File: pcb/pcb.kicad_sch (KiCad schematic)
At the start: 90 parts, among them J1 OLED, SW1 RotaryEncoder_Switch, U1 Elite-C

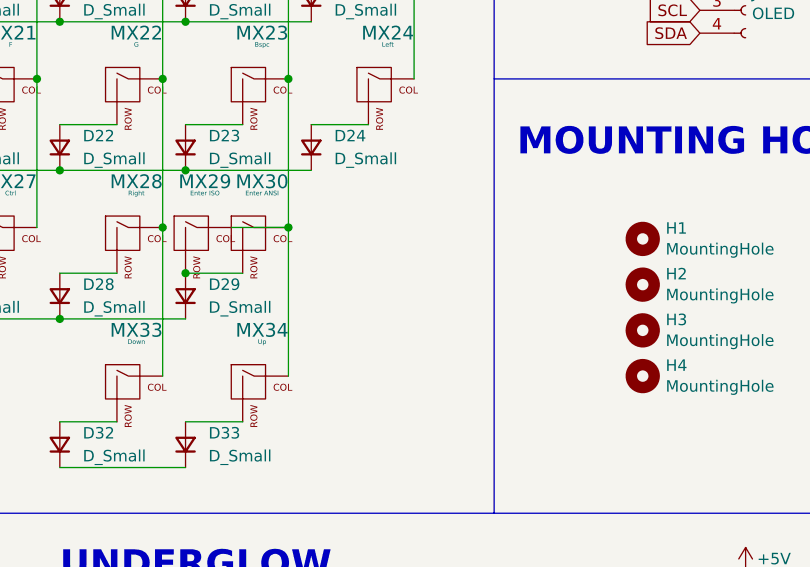
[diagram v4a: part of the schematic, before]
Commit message: Added footprints for most of the parts to the PCB file.
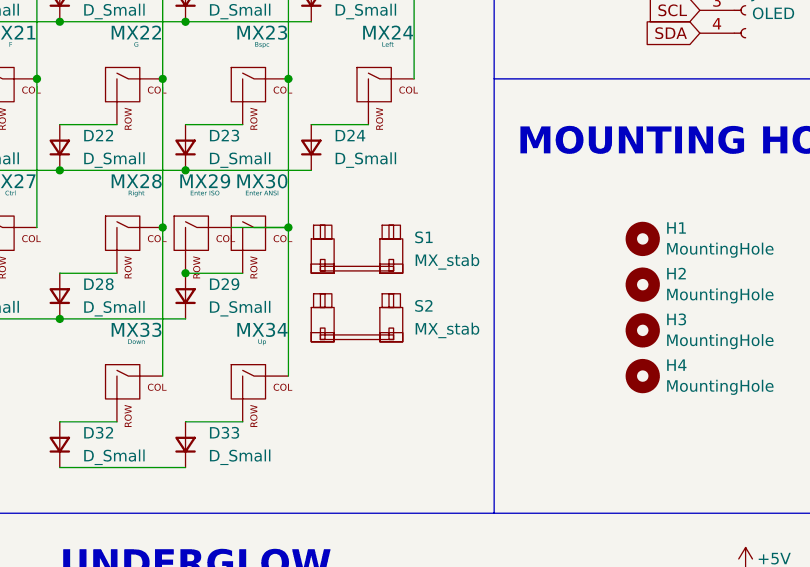
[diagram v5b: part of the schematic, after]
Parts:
- added S1: MX_stab, marbastlib-mx:STAB_MX_2.25u, symbol marbastlib-mx:MX_stab
- added S2: MX_stab, marbastlib-mx:STAB_MX_ISO_FLIPPED, symbol marbastlib-mx:MX_stab
- MX13, MX25, MX32: footprint acheron_MXH_metalrings:MX100H -> acheron_MXH_metalrings:MX125H
- MX26: footprint acheron_MXH_metalrings:MX100H -> acheron_MXH_metalrings:MX200H
- SW1: footprint Rotary_Encoder:RotaryEncoder_Alps_EC11E-Switch_Vertical_H20mm -> Keebio-Parts:RotaryEncoder_EC11-no-legs
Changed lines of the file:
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@@
       (effects (font (size 0.508 0.508)))
     )
-    (property "Footprint" "acheron_MXH_metalrings:MX100H" (id 2) (at 38.735 104.775 0)
+    (property "Footprint" "acheron_MXH_metalrings:MX200H" (id 2) (at 38.735 104.775 0)
       (effects (font (size 1.524 1.524)) hide)
     )
@@
     (pin "2")
   )
+  (symbol (lib_id "marbastlib-mx:MX_stab") (at 107.95 113.03 0) (unit 1)
+    (in_bom yes) (on_board yes) (fields_autoplaced)
+    (property "Reference" "S2" (id 0) (at 114.3 111.6329 0)
+      (effects (font (size 1.27 1.27)) (justify left))
+    )
+    (property "Value" "MX_stab" (id 1) (at 114.3 114.1729 0)
+      (effects (font (size 1.27 1.27)) (justify left))
+    )
+    (property "Footprint" "marbastlib-mx:STAB_MX_ISO_FLIPPED" (id 2) (at 107.95 113.03 0)
+      (effects (font (size 1.27 1.27)) hide)
+    )
+    (property "Datasheet" "" (id 3) (at 107.95 113.03 0)
+      (effects (font (size 1.27 1.27)) hide)
+    )
+  )
   (symbol (lib_id "MX_Alps_Hybrid:MX-NoLED") (at 96.52 54.61 0) (unit 1)
     (in_bom yes) (on_board yes) (fields_autoplaced)
@@
       (effects (font (size 0.508 0.508)))
     )
-    (property "Footprint" "acheron_MXH_metalrings:MX100H" (id 2) (at 24.765 71.755 0)
+    (property "Footprint" "acheron_MXH_metalrings:MX125H" (id 2) (at 24.765 71.755 0)
       (effects (font (size 1.524 1.524)) hide)
     )
@@
       (effects (font (size 0.508 0.508)))
     )
-    (property "Footprint" "acheron_MXH_metalrings:MX100H" (id 2) (at 24.765 104.775 0)
+    (property "Footprint" "acheron_MXH_metalrings:MX125H" (id 2) (at 24.765 104.775 0)
       (effects (font (size 1.524 1.524)) hide)
     )
@@
     (pin "1")
   )
+  (symbol (lib_id "marbastlib-mx:MX_stab") (at 107.95 105.41 0) (unit 1)
+    (in_bom yes) (on_board yes) (fields_autoplaced)
+    (property "Reference" "S1" (id 0) (at 114.3 104.0129 0)
+      (effects (font (size 1.27 1.27)) (justify left))
+    )
+    (property "Value" "MX_stab" (id 1) (at 114.3 106.5529 0)
+      (effects (font (size 1.27 1.27)) (justify left))
+    )
+    (property "Footprint" "marbastlib-mx:STAB_MX_2.25u" (id 2) (at 107.95 105.41 0)
+      (effects (font (size 1.27 1.27)) hide)
+    )
+    (property "Datasheet" "" (id 3) (at 107.95 105.41 0)
+      (effects (font (size 1.27 1.27)) hide)
+    )
+  )
   (symbol (lib_id "power:+5V") (at 151.13 140.97 0) (unit 1)
     (in_bom yes) (on_board yes)
@@
     (property "Reference" "SW1" (id 0) (at 144.78 30.48 0))
     (property "Value" "RotaryEncoder_Switch" (id 1) (at 144.78 33.02 0))
-    (property "Footprint" "Rotary_Encoder:RotaryEncoder_Alps_EC11E-Switch_Vertical_H20mm" (id 2) (at 148.59 44.704 0)
+    (property "Footprint" "Keebio-Parts:RotaryEncoder_EC11-no-legs" (id 2) (at 148.59 44.704 0)
       (effects (font (size 1.27 1.27)) hide)
     )
@@
       (effects (font (size 0.508 0.508)))
     )
-    (property "Footprint" "acheron_MXH_metalrings:MX100H" (id 2) (at 38.735 121.285 0)
+    (property "Footprint" "acheron_MXH_metalrings:MX125H" (id 2) (at 38.735 121.285 0)
       (effects (font (size 1.524 1.524)) hide)
     )
@@
     )
     (path "/3152788b-a0de-4109-8434-55ba1d4fe4a7"
-      (reference "MX13") (unit 1) (value "Shift") (footprint "acheron_MXH_metalrings:MX100H")
+      (reference "MX13") (unit 1) (value "Shift") (footprint "acheron_MXH_metalrings:MX125H")
     )
     (path "/46877c3a-ead4-41c8-afcb-24c8e59e5bae"
@@
     )
     (path "/553d3b6b-36a3-45b9-a24e-6f1c7c1abfbb"
-      (reference "MX25") (unit 1) (value "Alt") (footprint "acheron_MXH_metalrings:MX100H")
+      (reference "MX25") (unit 1) (value "Alt") (footprint "acheron_MXH_metalrings:MX125H")
     )
     (path "/152b7b17-3a42-4de5-b9bc-bdd22f42c43b"
-      (reference "MX26") (unit 1) (value "Space") (footprint "acheron_MXH_metalrings:MX100H")
+      (reference "MX26") (unit 1) (value "Space") (footprint "acheron_MXH_metalrings:MX200H")
     )
     (path "/d49df2b5-b3d2-431c-82f1-b1e8d86ff7d8"
@@
     )
     (path "/e3b59c53-ccff-4bc2-b7b7-efe6efe4c5cc"
-      (reference "MX32") (unit 1) (value "Alt") (footprint "acheron_MXH_metalrings:MX100H")
+      (reference "MX32") (unit 1) (value "Alt") (footprint "acheron_MXH_metalrings:MX125H")
     )
     (path "/5b6c7f1e-f125-477d-8e10-4610f8169c66"
@@
       (reference "MX34") (unit 1) (value "Up") (footprint "acheron_MXH_metalrings:MX100H")
     )
+    (path "/7ed119b7-b4ae-4245-9c6d-905d8f015e10"
+      (reference "S1") (unit 1) (value "MX_stab") (footprint "marbastlib-mx:STAB_MX_2.25u")
+    )
+    (path "/2fce2717-c9bf-487d-a03f-ec3953ab514e"
+      (reference "S2") (unit 1) (value "MX_stab") (footprint "marbastlib-mx:STAB_MX_ISO_FLIPPED")
+    )
     (path "/b0099de3-5821-425e-97d9-b89f55184911"
-      (reference "SW1") (unit 1) (value "RotaryEncoder_Switch") (footprint "Rotary_Encoder:RotaryEncoder_Alps_EC11E-Switch_Vertical_H20mm")
+      (reference "SW1") (unit 1) (value "RotaryEncoder_Switch") (footprint "Keebio-Parts:RotaryEncoder_EC11-no-legs")
     )
     (path "/45e43045-7dd0-4e88-82a6-613fa4322bc2"

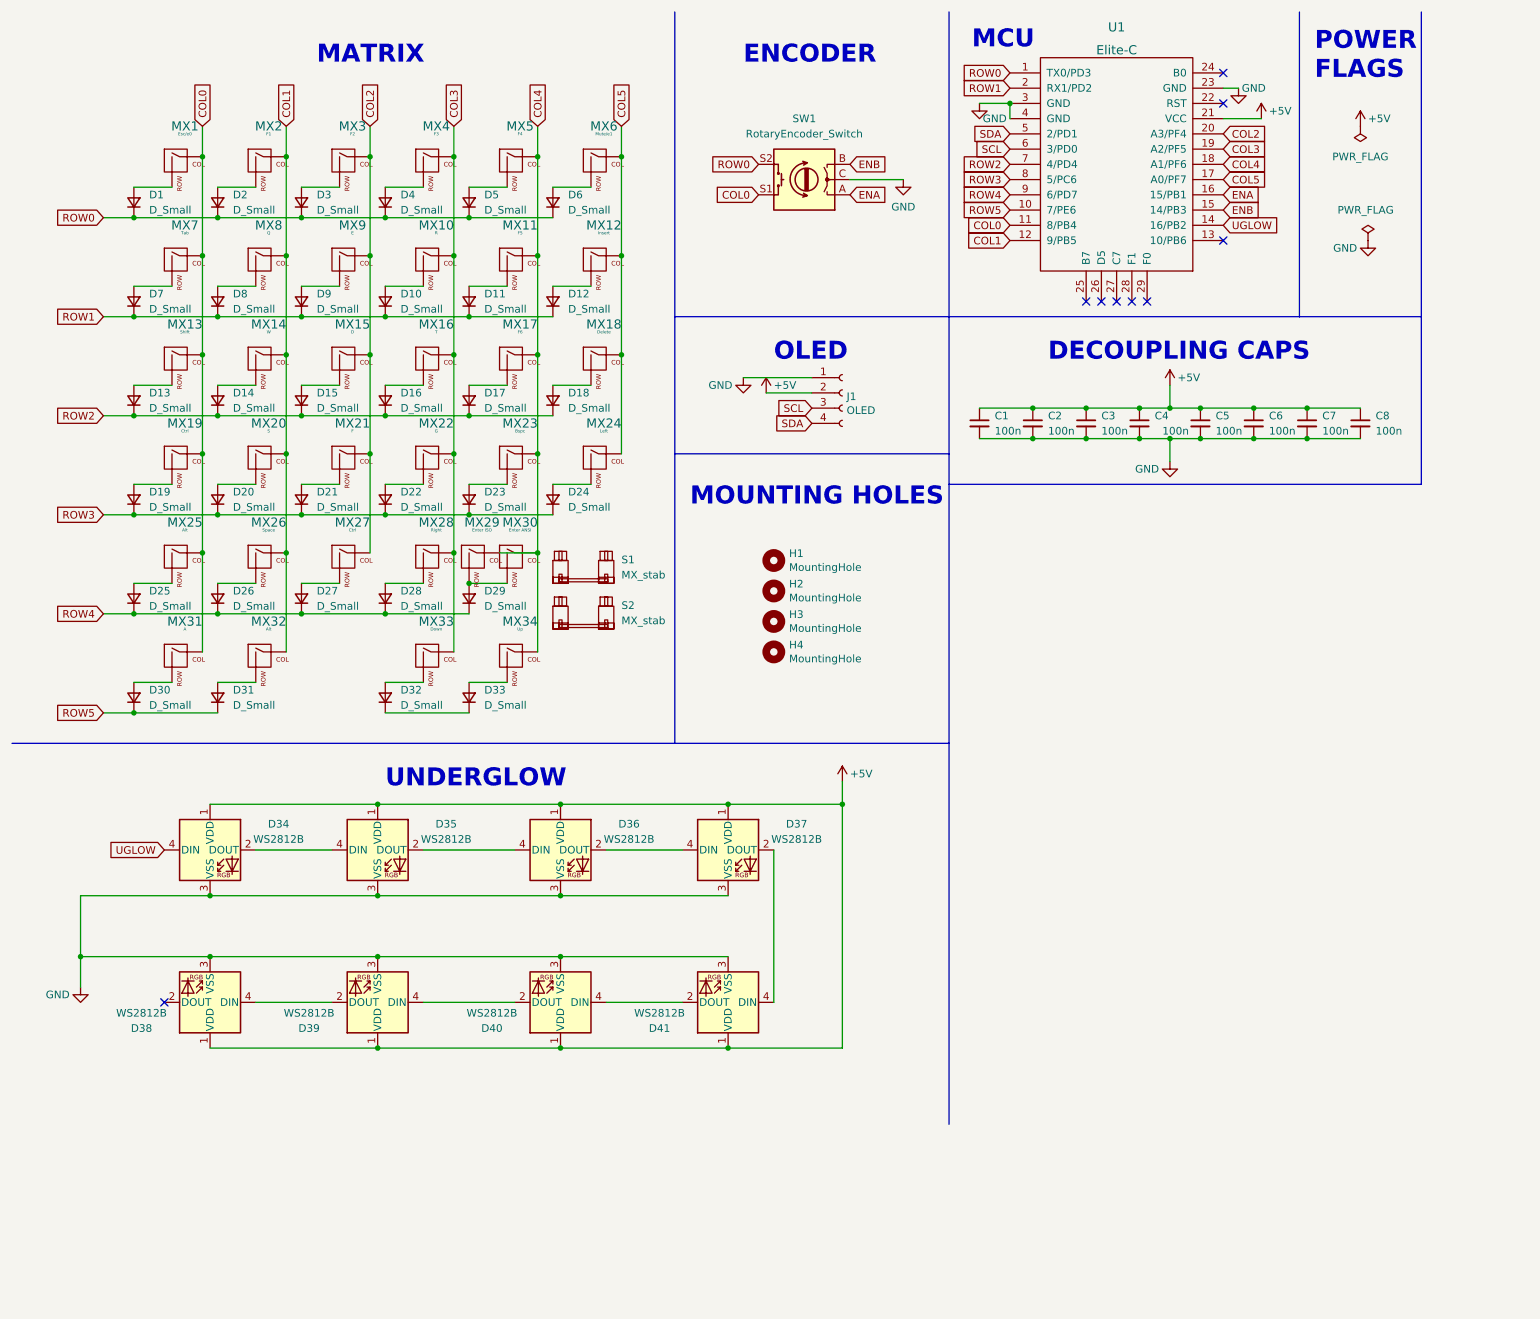
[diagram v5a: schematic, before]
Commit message: Added missing LEDs and caps.
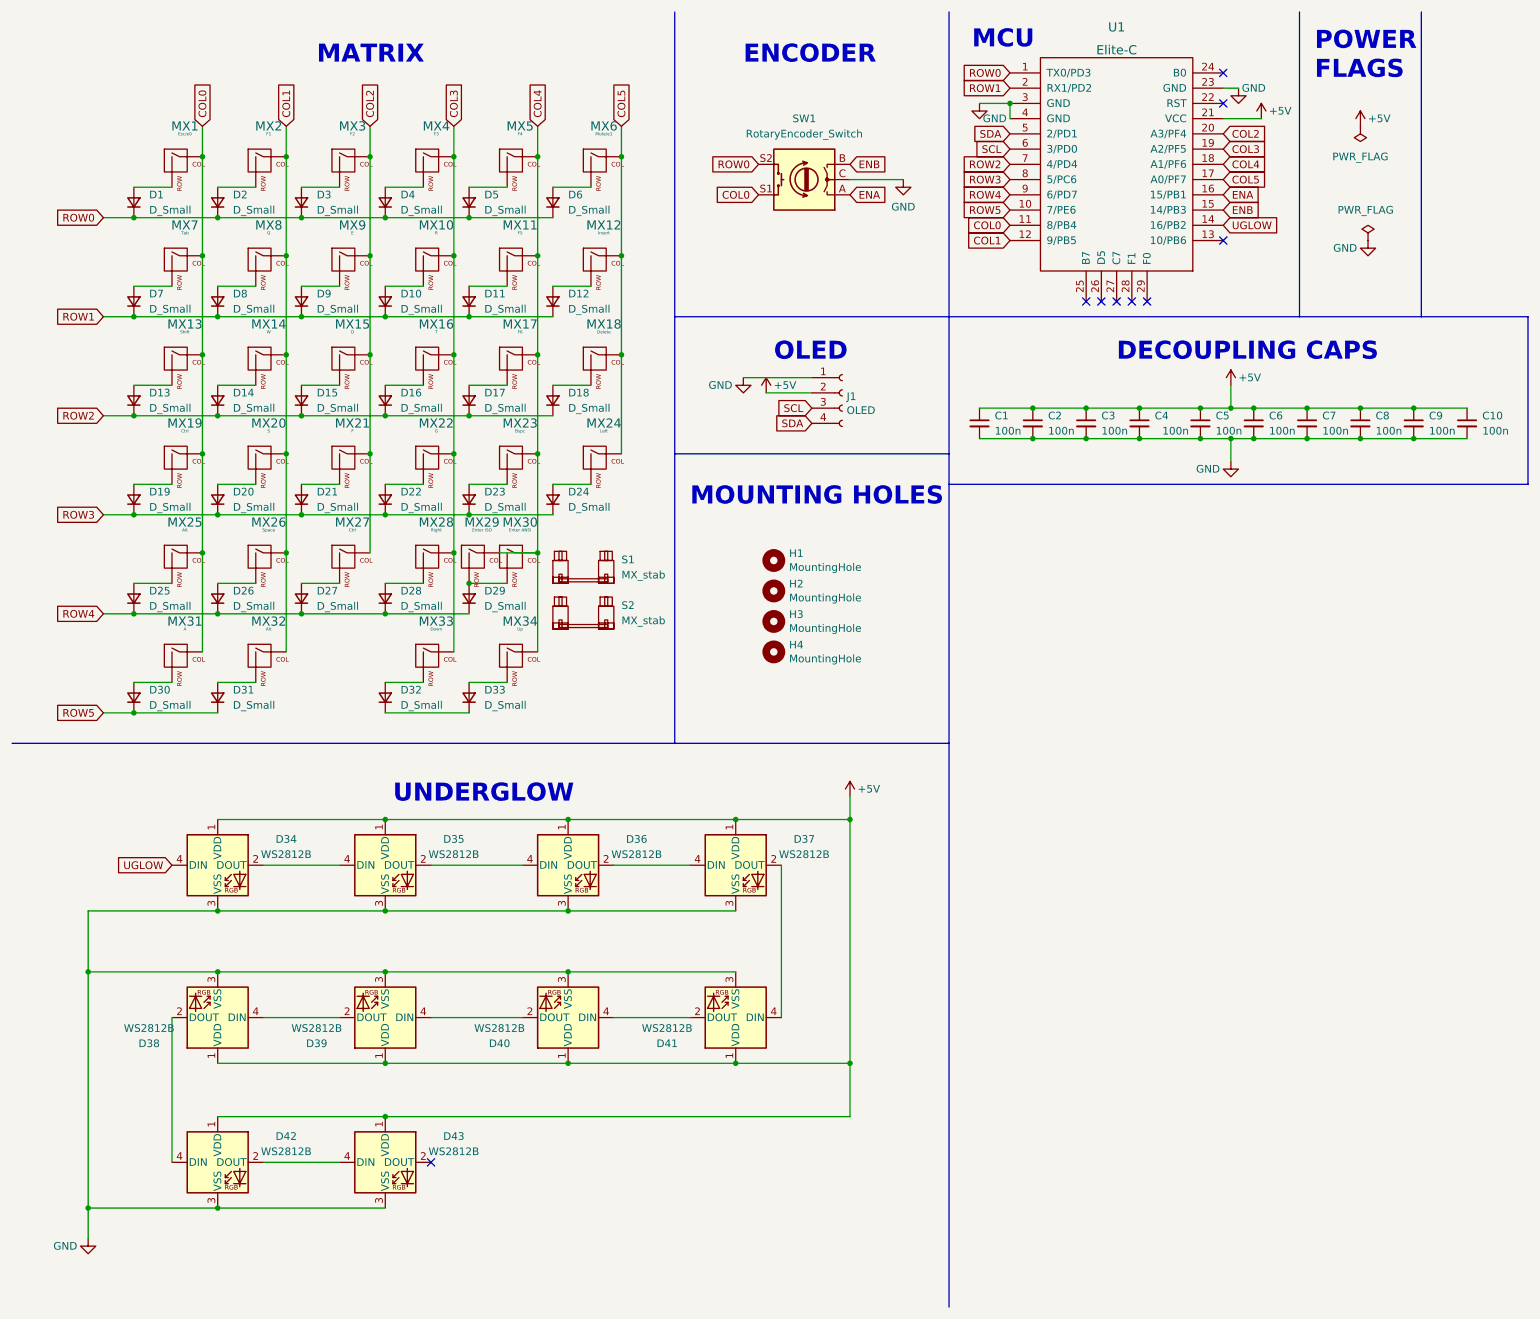
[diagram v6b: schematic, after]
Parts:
- added C10, C9: 100n, Capacitor_SMD:C_0805_2012Metric_Pad1.18x1.45mm_HandSolder, symbol Device:C_Small
- added D42, D43: WS2812B, LED_SMD:LED_WS2812B_PLCC4_5.0x5.0mm_P3.2mm, symbol LED:WS2812B
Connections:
- net +5V: now also C10.1, C9.1, D42.1 (VDD), D43.1 (VDD)
- net GND: now also C10.2, C9.2, D42.3 (VSS), D43.3 (VSS)
- net at D38.2 (DOUT): now also D42.4 (DIN)
- new net: D42.2 (DOUT), D43.4 (DIN)
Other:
- moved on the sheet: D34, D35, D36, D37, D38, D39, D40, D41

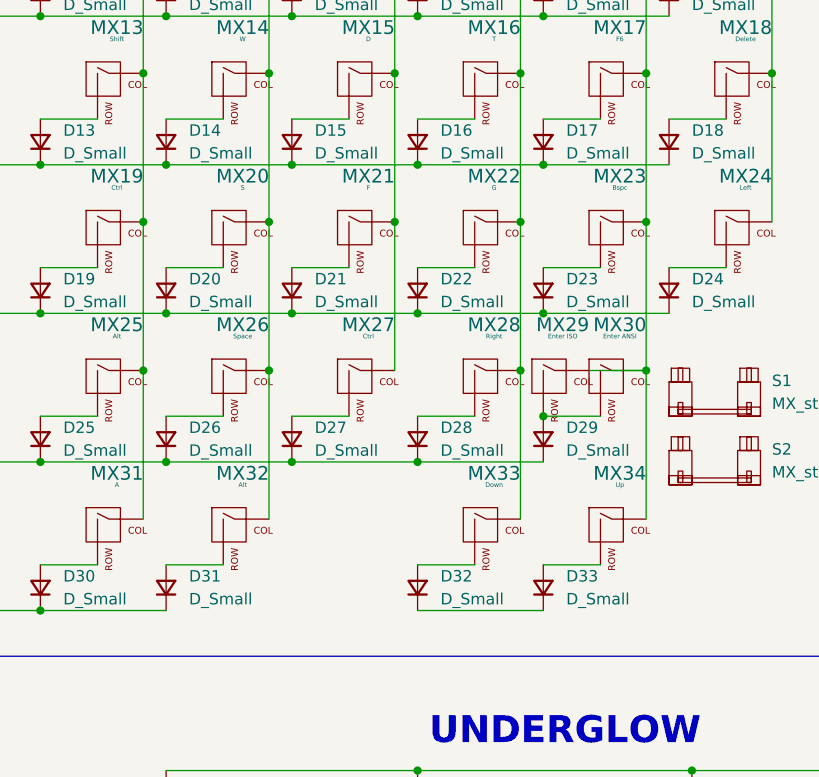
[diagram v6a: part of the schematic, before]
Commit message: Routed power and switch matrix. Pending connections to the MCU.
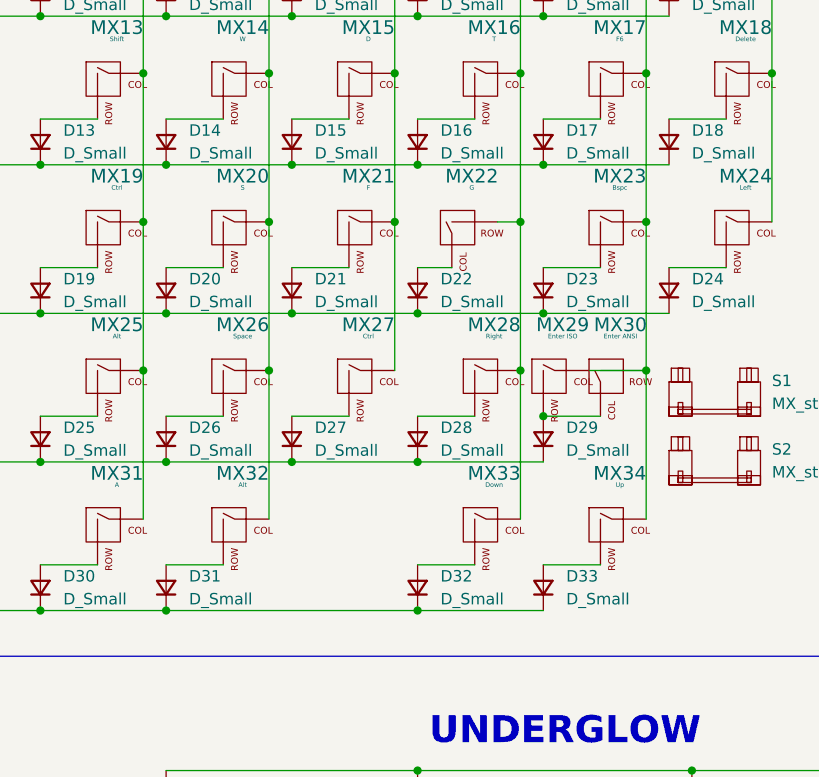
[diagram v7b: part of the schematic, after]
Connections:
- net COL3: now also MX22.2 (ROW); no longer MX22.1 (COL)
- net COL4: now also MX30.2 (ROW); no longer MX30.1 (COL)
- net ROW5: now also D32.1 (K), D33.1 (K)
- net at D29.2 (A), MX29.2 (ROW): now also MX30.1 (COL); no longer MX30.2 (ROW)
- net at D22.2 (A): now also MX22.1 (COL); no longer MX22.2 (ROW)
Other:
- moved on the sheet: MX22, MX30
